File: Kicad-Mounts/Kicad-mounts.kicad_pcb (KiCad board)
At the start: 2 copper layers, 25 x 35.8 mm, 8 parts, among them P3 CONN_6X2, P6 CONN_3, U2 TPS77033

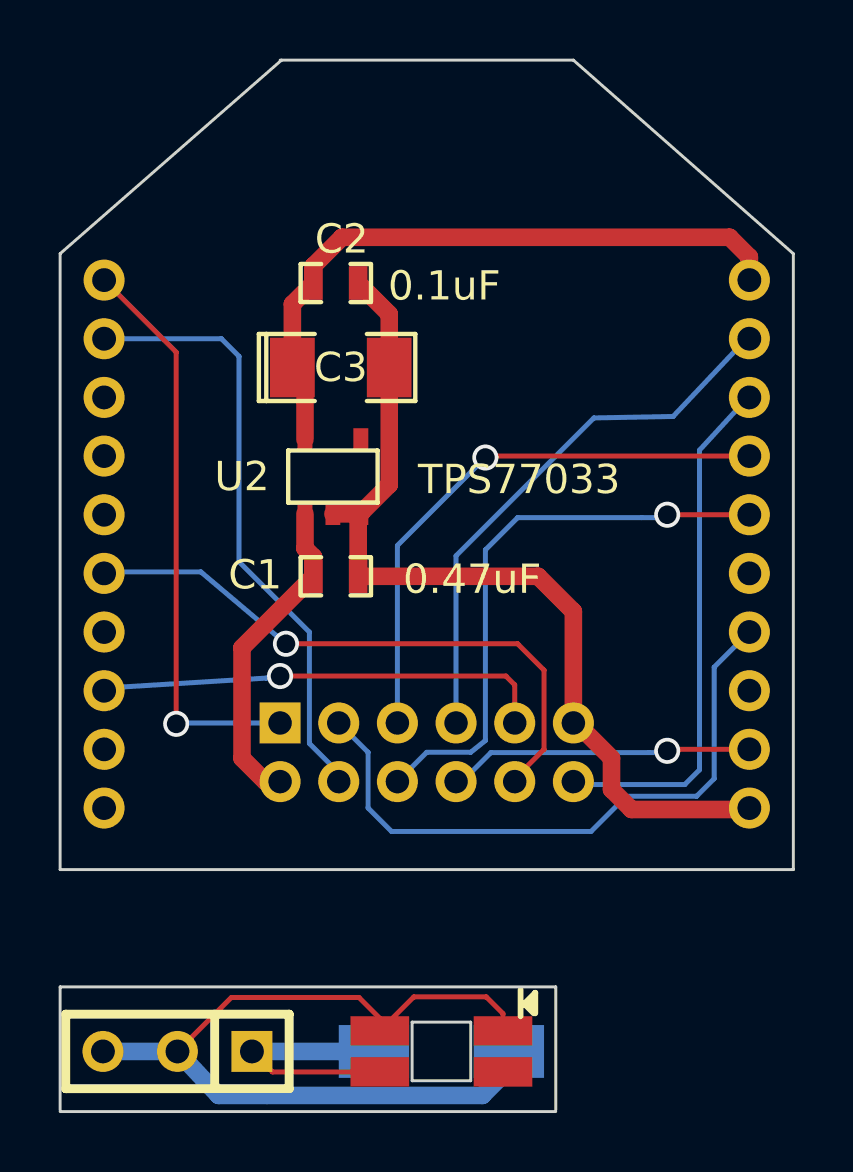
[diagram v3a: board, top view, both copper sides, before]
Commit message: Small change to Kicad_mounts to allow possibility of a SMD connector.
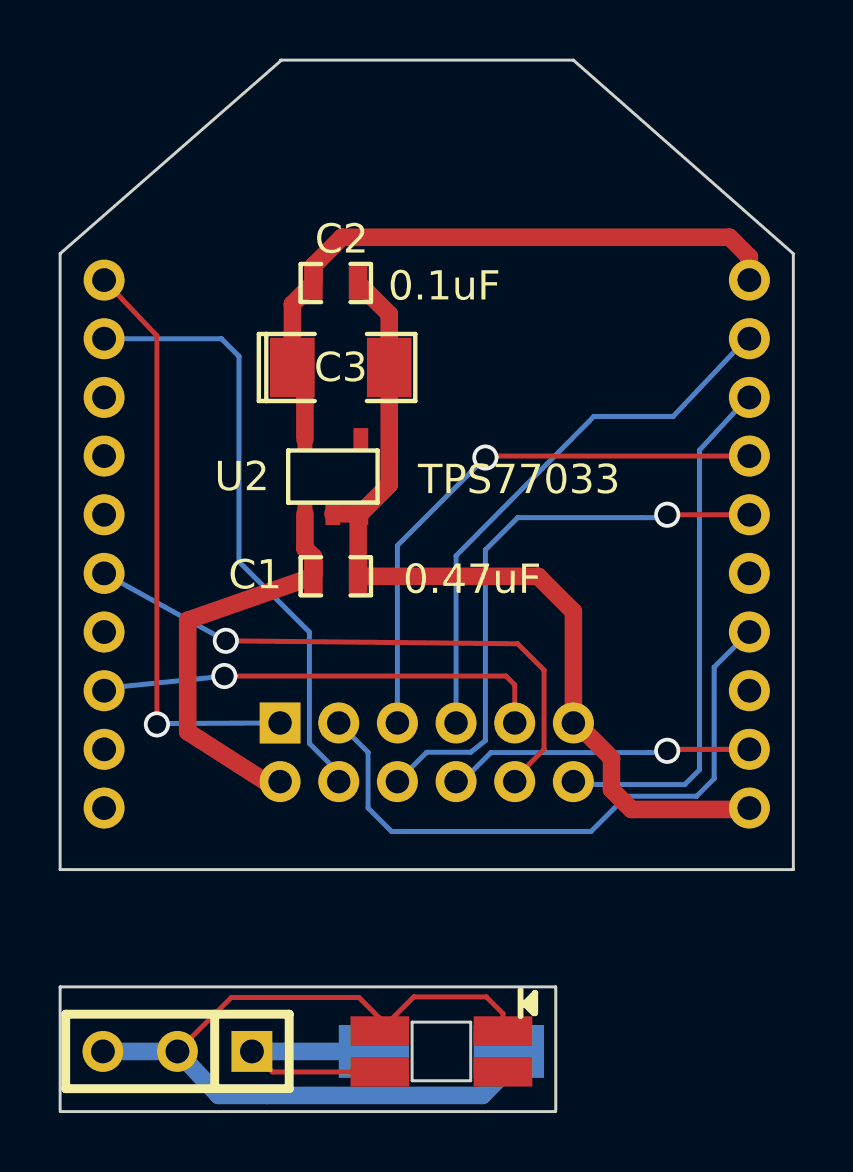
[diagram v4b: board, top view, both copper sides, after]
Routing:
- net VCC: track 11.1 -> 14.2 mm
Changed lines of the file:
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@@
   (segment (start 176.638 107.338) (end 176.3475 107.0475) (width 0.6) (layer F.Cu) (net 3))
   (segment (start 175.5 115) (end 175 115) (width 0.6) (layer F.Cu) (net 3))
-  (segment (start 175 115) (end 174.2 114.2) (width 0.6) (layer F.Cu) (net 3))
-  (segment (start 174.2 114.2) (end 174.2 110.438) (width 0.6) (layer F.Cu) (net 3))
-  (segment (start 174.2 110.438) (end 176.638 108) (width 0.6) (layer F.Cu) (net 3))
+  (segment (start 175 115) (end 172.35 113.3) (width 0.6) (layer F.Cu) (net 3))
+  (segment (start 172.35 113.3) (end 172.35 109.5) (width 0.6) (layer F.Cu) (net 3))
+  (segment (start 172.35 109.5) (end 176.638 108) (width 0.6) (layer F.Cu) (net 3))
   (segment (start 191.50074 101.9005) (end 191.2105 101.9005) (width 0.17) (layer F.Cu) (net 4))
   (segment (start 191.4 101.95) (end 191.4 101.96) (width 0.17) (layer B.Cu) (net 4))
@@
   (segment (start 189.8 103.7) (end 189.8 114.6) (width 0.17) (layer B.Cu) (net 4))
   (segment (start 191.50074 99.89898) (end 191.50074 99.65074) (width 0.17) (layer F.Cu) (net 5))
-  (segment (start 186.2 102.6) (end 188.9 102.55) (width 0.17) (layer B.Cu) (net 5))
+  (segment (start 186.2 102.55) (end 188.9 102.55) (width 0.17) (layer B.Cu) (net 5))
   (segment (start 188.9 102.55) (end 191.45 99.85) (width 0.17) (layer B.Cu) (net 5))
   (segment (start 181.5 113) (end 181.5 107.3) (width 0.17) (layer B.Cu) (net 5))
-  (segment (start 186.2 102.6) (end 181.5 107.3) (width 0.17) (layer B.Cu) (net 5))
+  (segment (start 186.2 102.55) (end 181.5 107.3) (width 0.17) (layer B.Cu) (net 5))
   (segment (start 179.5 113) (end 179.5 106.95) (width 0.17) (layer B.Cu) (net 6))
   (segment (start 182.55052 103.89948) (end 191.50074 103.89948) (width 0.17) (layer F.Cu) (net 6))
@@
   (segment (start 169.92974 111.47) (end 169.49926 111.90048) (width 0.17) (layer F.Cu) (net 13))
   (segment (start 183.5 113) (end 183.5 111.7) (width 0.17) (layer F.Cu) (net 13))
-  (segment (start 175.03 111.47) (end 169.7 111.8) (width 0.17) (layer B.Cu) (net 13))
-  (segment (start 175.5 111.4) (end 175.03 111.47) (width 0.17) (layer B.Cu) (net 13))
-  (via (at 175.5 111.4) (size 0.889) (drill 0.635) (layers F.Cu B.Cu) (net 13))
-  (segment (start 183.2 111.4) (end 175.6 111.4) (width 0.17) (layer F.Cu) (net 13))
+  (segment (start 173.65 111.4) (end 169.7 111.8) (width 0.17) (layer B.Cu) (net 13))
+  (segment (start 173.6 111.4) (end 173.65 111.4) (width 0.17) (layer B.Cu) (net 13))
+  (via (at 173.6 111.4) (size 0.889) (drill 0.635) (layers F.Cu B.Cu) (net 13))
+  (segment (start 183.2 111.4) (end 173.7 111.4) (width 0.17) (layer F.Cu) (net 13))
   (segment (start 183.5 111.7) (end 183.2 111.4) (width 0.17) (layer F.Cu) (net 13))
   (segment (start 183.5 113) (end 183.5 113.2) (width 0.17) (layer F.Cu) (net 13))
@@
   (segment (start 184.5 113.9) (end 184.5 111.2) (width 0.17) (layer F.Cu) (net 17))
   (segment (start 184.5 111.2) (end 183.6 110.3) (width 0.17) (layer F.Cu) (net 17))
-  (segment (start 183.6 110.3) (end 175.7 110.3) (width 0.17) (layer F.Cu) (net 17))
-  (via (at 175.7 110.3) (size 0.889) (drill 0.635) (layers F.Cu B.Cu) (net 17))
-  (segment (start 175.7 110.3) (end 172.8 107.85) (width 0.17) (layer B.Cu) (net 17))
-  (segment (start 172.8 107.85) (end 169.45 107.85) (width 0.17) (layer B.Cu) (net 17))
-  (segment (start 175.5 113) (end 171.988 113) (width 0.17) (layer B.Cu) (net 18))
-  (segment (start 171.958 100.35874) (end 169.49926 97.9) (width 0.17) (layer F.Cu) (net 18))
-  (segment (start 171.958 113.03) (end 171.958 100.35874) (width 0.17) (layer F.Cu) (net 18))
-  (segment (start 171.958 113.03) (end 171.958 113.03) (width 0.17) (layer F.Cu) (net 18))
-  (via (at 171.958 113.03) (size 0.889) (drill 0.635) (layers F.Cu B.Cu) (net 18))
-  (segment (start 171.988 113) (end 171.958 113.03) (width 0.17) (layer B.Cu) (net 18))
+  (segment (start 183.6 110.3) (end 173.65 110.2) (width 0.17) (layer F.Cu) (net 17))
+  (via (at 173.65 110.2) (size 0.889) (drill 0.635) (layers F.Cu B.Cu) (net 17))
+  (segment (start 173.65 110.2) (end 169.5 107.9) (width 0.17) (layer B.Cu) (net 17))
+  (segment (start 169.5 107.9) (end 169.45 107.85) (width 0.17) (layer B.Cu) (net 17))
+  (segment (start 175.5 113) (end 171.33 113.02) (width 0.17) (layer B.Cu) (net 18))
+  (segment (start 171.3 99.8) (end 169.49926 97.9) (width 0.17) (layer F.Cu) (net 18))
+  (segment (start 171.3 113.05) (end 171.3 99.8) (width 0.17) (layer F.Cu) (net 18))
+  (segment (start 171.3 113.05) (end 171.3 113.05) (width 0.17) (layer F.Cu) (net 18))
+  (via (at 171.3 113.05) (size 0.889) (drill 0.635) (layers F.Cu B.Cu) (net 18))
+  (segment (start 171.33 113.02) (end 171.3 113.05) (width 0.17) (layer B.Cu) (net 18))
   (segment (start 169.49926 101.9005) (end 169.7095 101.9005) (width 0.17) (layer F.Cu) (net 20))
 )
